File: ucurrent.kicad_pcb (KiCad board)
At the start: 2 copper layers, 41.9 x 64.9 mm, 38 parts, among them J1 Conn_01x02, J2 IN_P, J3 IN_N, J4 POWER, J5 Select, J6 OUT_P, J7 OUT_N, SW1 BAT_TEST, U1 TPS3839DBZ, U2 LMV321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

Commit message: Readme, github on silkscreen
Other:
- board text added: "2019-11-06"
- board text added: "https://github.com/NerdyProjects/ucurrent-clone"
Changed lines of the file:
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@@
   (general
     (thickness 1.6)
-    (drawings 21)
+    (drawings 23)
     (tracks 203)
     (zones 0)
@@
     )
   )
+  (gr_text 2019-11-06 (at 119.634 41.5544) (layer B.SilkS)
+    (effects (font (size 0.8 0.8) (thickness 0.15)) (justify mirror))
+  )
+  (gr_text https://github.com/NerdyProjects/ucurrent-clone (at 122.8344 70.7644 90) (layer B.SilkS)
+    (effects (font (size 0.8 0.8) (thickness 0.15)) (justify mirror))
+  )
   (gr_text "+/-\n0-1250 mV" (at 82.4992 66.5988) (layer F.SilkS)

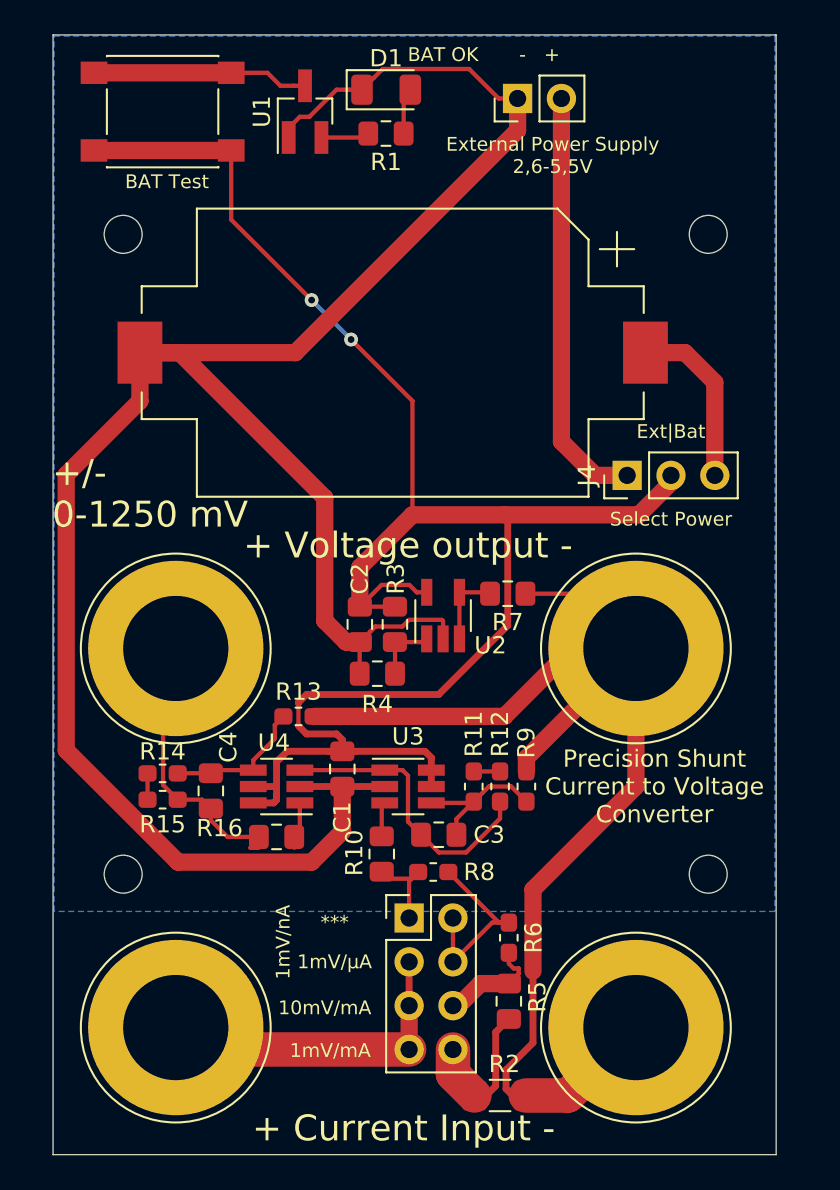
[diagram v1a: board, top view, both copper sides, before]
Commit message: Allow mounting of PCB top or bottom up
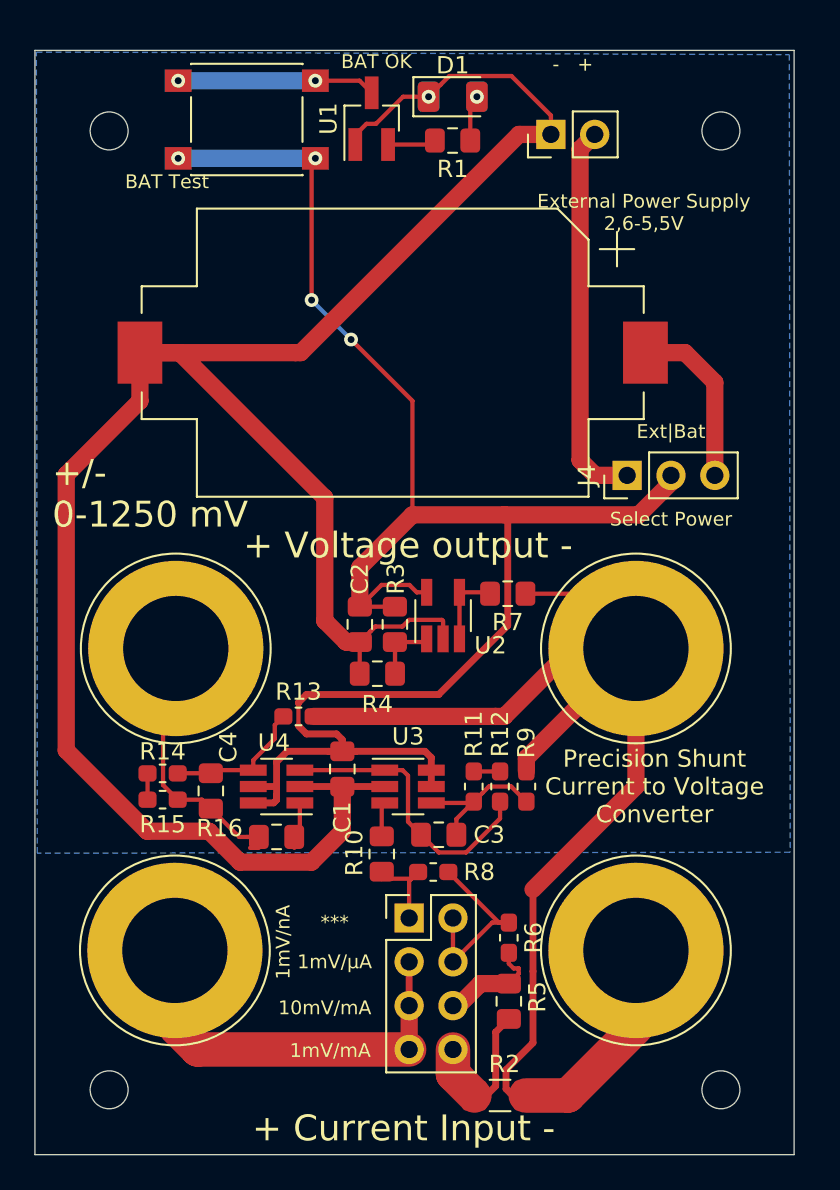
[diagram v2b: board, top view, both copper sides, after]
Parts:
- added D2: GREEN, LED_SMD:LED_1206_3216Metric, B.Cu at (105.7, 43.6)
- added SW2: BAT_TEST, Button_Switch_SMD:SW_Push_1P1T_NO_6x6mm_H9.5mm, B.Cu at (93.8, 44.9)
- moved H4 12.5 mm to (85.8, 101.1)
- moved H3 12.5 mm to (121.3, 101.1)
- moved H2 6.05 mm to (85.8, 45.6)
- moved H1 6.04 mm to (121.3, 45.6)
- moved SW1 4.90 mm to (93.8, 44.9)
- moved J2 4.47 mm to (89.6, 93.1)
- moved J3 4.47 mm to (116.3, 93.1)
- moved D1 3.88 mm to (105.7, 43.6)
- moved R1 3.88 mm to (105.7, 46.1)
- moved U1 3.88 mm to (101.0, 44.9)
- moved J1 2.84 mm to (111.4, 45.8)
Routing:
- net Net-(J2-Pad1): track 23.8 -> 20.7 mm
- net +VDC: track 104.2 -> 101.9 mm, vias 2 -> 4
- net Net-(J1-Pad2): track 24.5 -> 22.3 mm
- net Net-(SW1-Pad1): track 12.5 -> 11.5 mm, vias 0 -> 2
- net -VDC: track 128.9 -> 128.2 mm, vias 0 -> 1
- net Net-(D1-Pad2): vias 0 -> 1
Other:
- board size 41.9 x 64.9 mm -> 44 x 64 mm
- board text added: "+ -"
- board text added: "- Current Input +"
- board text added: "- Voltage output +"
- board text added: "Bat|Ext"
- board text added: "heavily inspired from µCurrent gold (see eevblog.com). This device does not provide same accuracy or comfort of use as the original. Use of cheaper sense and opamp resistors should lead to +/-1% accuracy on all ranges. Temperature drift should be < 50 ppm, offset voltage and bandwidth unaffected from original (< 50µV, > 300 kHz)"
- board text removed: "heavily inspired from µCurrent gold (see eevblog.com). This device does not provide same accuracy or comfort of use as the original. Use of cheaper sense and opamp resistors should lead to ~+/-1% accuracy on all ranges. Temperature drift should be < 50 ppm, offset voltage and bandwidth unaffected from original (< 50µV, > 300 kHz)"

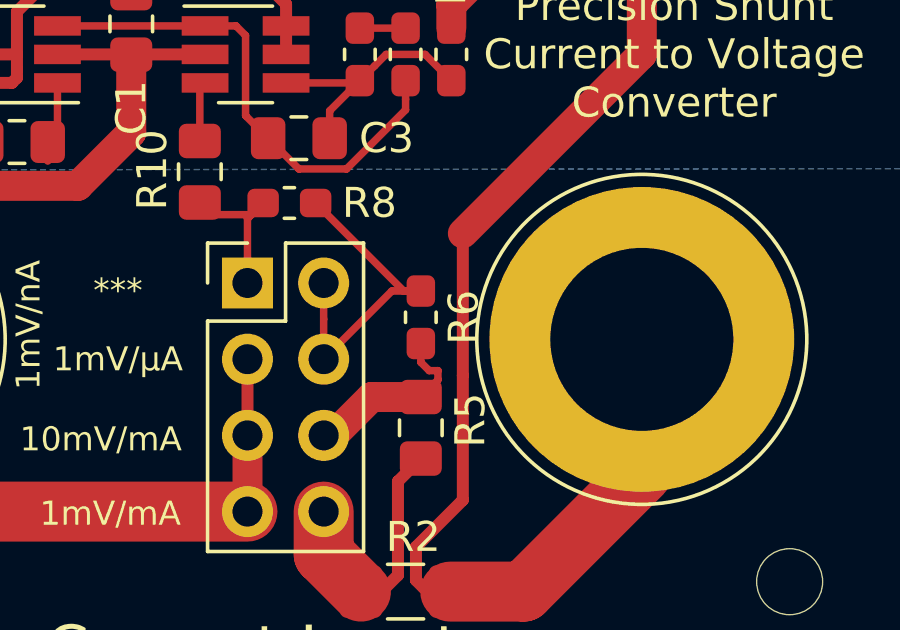
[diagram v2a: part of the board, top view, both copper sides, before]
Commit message: update part list, fix footprint
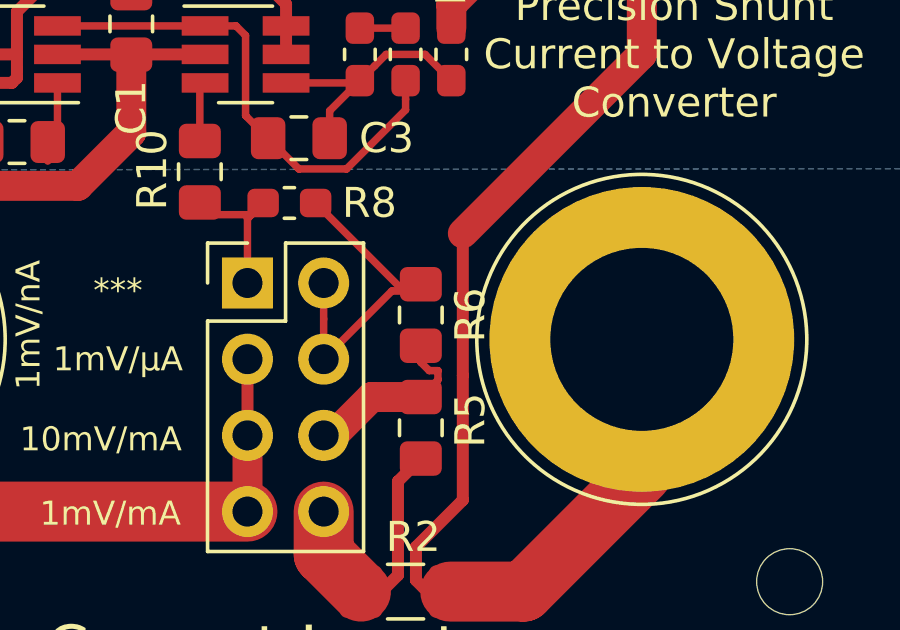
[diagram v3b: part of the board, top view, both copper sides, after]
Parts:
- R6: footprint Resistor_SMD:R_0603_1608Metric_Pad1.05x0.95mm_HandSolder -> Resistor_SMD:R_0805_2012Metric_Pad1.15x1.40mm_HandSolder
- moved R6 0.08 mm to (109.0, 92.3)
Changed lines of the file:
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@@
     (add_net "Net-(SW1-Pad1)")
+  )
+  (module Resistor_SMD:R_0805_2012Metric_Pad1.15x1.40mm_HandSolder (layer F.Cu)
+    (at 108.966 92.2528 270)
+    (descr "Resistor SMD 0805 (2012 Metric), square (rectangular) end terminal, IPC_7351 nominal with elongated pad for handsoldering. (Body size source: https://docs.google.com/spreadsheets/d/1BsfQQcO9C6DZCsRaXUlFlo91Tg2WpOkGARC1WS5S8t0/edit?usp=sharing), generated with kicad-footprint-generator")
+    (tags "resistor handsolder")
+    (attr smd)
+    (fp_text reference R6 (at 0 -1.65 90) (layer F.SilkS)
+      (effects (font (size 1 1) (thickness 0.15)))
+    )
+    (fp_text value "10R 1%" (at 0 1.65 90) (layer F.Fab)
+      (effects (font (size 1 1) (thickness 0.15)))
+    )
+    (fp_text user %R (at 0 0 90) (layer F.Fab)
+      (effects (font (size 0.5 0.5) (thickness 0.08)))
+    )
+    (fp_line (start 1.85 0.95) (end -1.85 0.95) (layer F.CrtYd) (width 0.05))
+    (fp_line (start 1.85 -0.95) (end 1.85 0.95) (layer F.CrtYd) (width 0.05))
+    (fp_line (start -1.85 -0.95) (end 1.85 -0.95) (layer F.CrtYd) (width 0.05))
+    (fp_line (start -1.85 0.95) (end -1.85 -0.95) (layer F.CrtYd) (width 0.05))
+    (fp_line (start -0.261252 0.71) (end 0.261252 0.71) (layer F.SilkS) (width 0.12))
+    (fp_line (start -0.261252 -0.71) (end 0.261252 -0.71) (layer F.SilkS) (width 0.12))
+    (fp_line (start 1 0.6) (end -1 0.6) (layer F.Fab) (width 0.1))
+    (fp_line (start 1 -0.6) (end 1 0.6) (layer F.Fab) (width 0.1))
+    (fp_line (start -1 -0.6) (end 1 -0.6) (layer F.Fab) (width 0.1))
+    (fp_line (start -1 0.6) (end -1 -0.6) (layer F.Fab) (width 0.1))
+    (pad 2 smd roundrect (at 1.025 0 270) (size 1.15 1.4) (layers F.Cu F.Paste F.Mask) (roundrect_rratio 0.217391)
+      (net 12 "Net-(J5-Pad6)"))
+    (pad 1 smd roundrect (at -1.025 0 270) (size 1.15 1.4) (layers F.Cu F.Paste F.Mask) (roundrect_rratio 0.217391)
+      (net 13 "Net-(J5-Pad2)"))
+    (model ${KISYS3DMOD}/Resistor_SMD.3dshapes/R_0805_2012Metric.wrl
+      (at (xyz 0 0 0))
+      (scale (xyz 1 1 1))
+      (rotate (xyz 0 0 0))
+    )
   )
   (module Button_Switch_SMD:SW_Push_1P1T_NO_6x6mm_H9.5mm (layer B.Cu)
@@
       (at (xyz 0 0 0))
       (scale (xyz 1 1 1))
-      (rotate (xyz 0 0 0))
-    )
-  )
-  (module Resistor_SMD:R_0603_1608Metric_Pad1.05x0.95mm_HandSolder (layer F.Cu)
-    (at 108.966 92.329 270)
-    (descr "Resistor SMD 0603 (1608 Metric), square (rectangular) end terminal, IPC_7351 nominal with elongated pad for handsoldering. (Body size source: http://www.tortai-tech.com/upload/download/2011102023233369053.pdf), generated with kicad-footprint-generator")
-    (tags "resistor handsolder")
-    (attr smd)
-    (fp_text reference R6 (at 0 -1.43 90) (layer F.SilkS)
-      (effects (font (size 1 1) (thickness 0.15)))
-    )
-    (fp_text value "10R 1%" (at 0 1.43 90) (layer F.Fab)
-      (effects (font (size 1 1) (thickness 0.15)))
-    )
-    (fp_text user %R (at 0 0 90) (layer F.Fab)
-      (effects (font (size 0.4 0.4) (thickness 0.06)))
-    )
-    (fp_line (start 1.65 0.73) (end -1.65 0.73) (layer F.CrtYd) (width 0.05))
-    (fp_line (start 1.65 -0.73) (end 1.65 0.73) (layer F.CrtYd) (width 0.05))
-    (fp_line (start -1.65 -0.73) (end 1.65 -0.73) (layer F.CrtYd) (width 0.05))
-    (fp_line (start -1.65 0.73) (end -1.65 -0.73) (layer F.CrtYd) (width 0.05))
-    (fp_line (start -0.171267 0.51) (end 0.171267 0.51) (layer F.SilkS) (width 0.12))
-    (fp_line (start -0.171267 -0.51) (end 0.171267 -0.51) (layer F.SilkS) (width 0.12))
-    (fp_line (start 0.8 0.4) (end -0.8 0.4) (layer F.Fab) (width 0.1))
-    (fp_line (start 0.8 -0.4) (end 0.8 0.4) (layer F.Fab) (width 0.1))
-    (fp_line (start -0.8 -0.4) (end 0.8 -0.4) (layer F.Fab) (width 0.1))
-    (fp_line (start -0.8 0.4) (end -0.8 -0.4) (layer F.Fab) (width 0.1))
-    (pad 2 smd roundrect (at 0.875 0 270) (size 1.05 0.95) (layers F.Cu F.Paste F.Mask) (roundrect_rratio 0.25)
-      (net 12 "Net-(J5-Pad6)"))
-    (pad 1 smd roundrect (at -0.875 0 270) (size 1.05 0.95) (layers F.Cu F.Paste F.Mask) (roundrect_rratio 0.25)
-      (net 13 "Net-(J5-Pad2)"))
-    (model ${KISYS3DMOD}/Resistor_SMD.3dshapes/R_0603_1608Metric.wrl
-      (at (xyz 0 0 0))
-      (scale (xyz 1 1 1))
